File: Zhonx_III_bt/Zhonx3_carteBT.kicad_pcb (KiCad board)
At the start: 2 copper layers, 21.7 x 21.3 mm, 14 parts, among them P1 CONN_01X04, U2 SPBT2632C2A, U3 LP2992

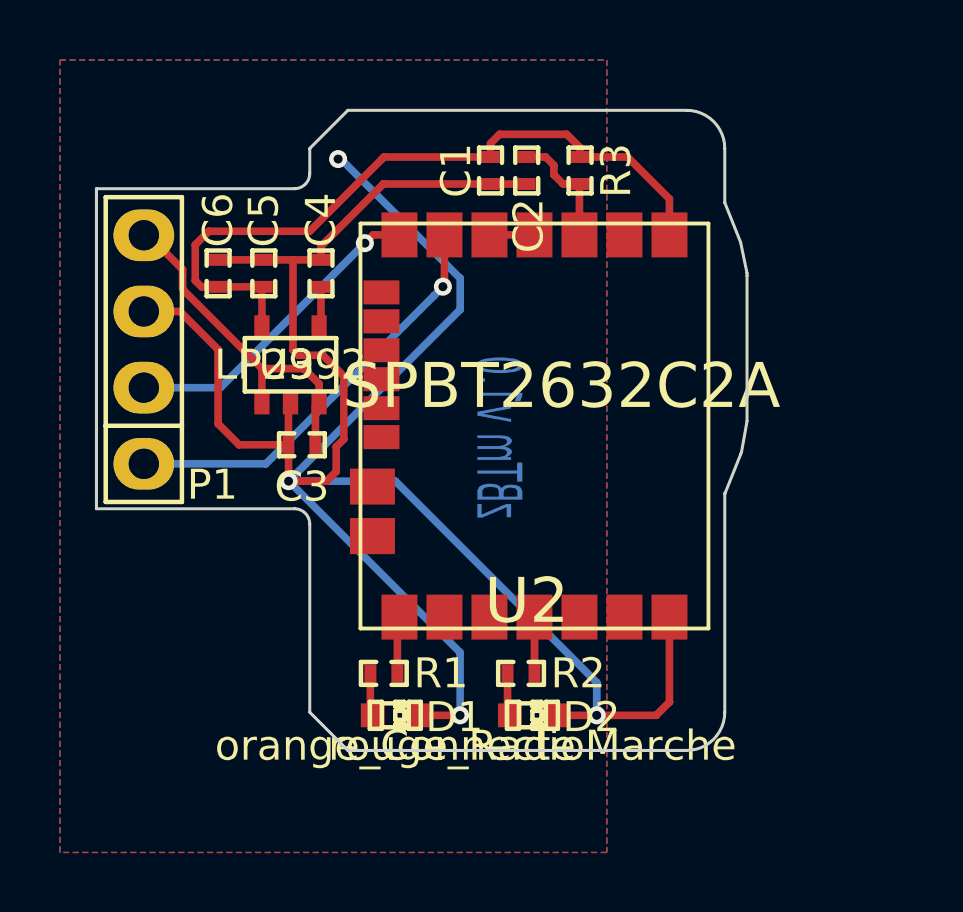
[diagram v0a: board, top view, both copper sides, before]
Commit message: bluetooth passage en 4 couches
Signed-off-by: Jean-Paul <pacabot.jbe@gmail.com>
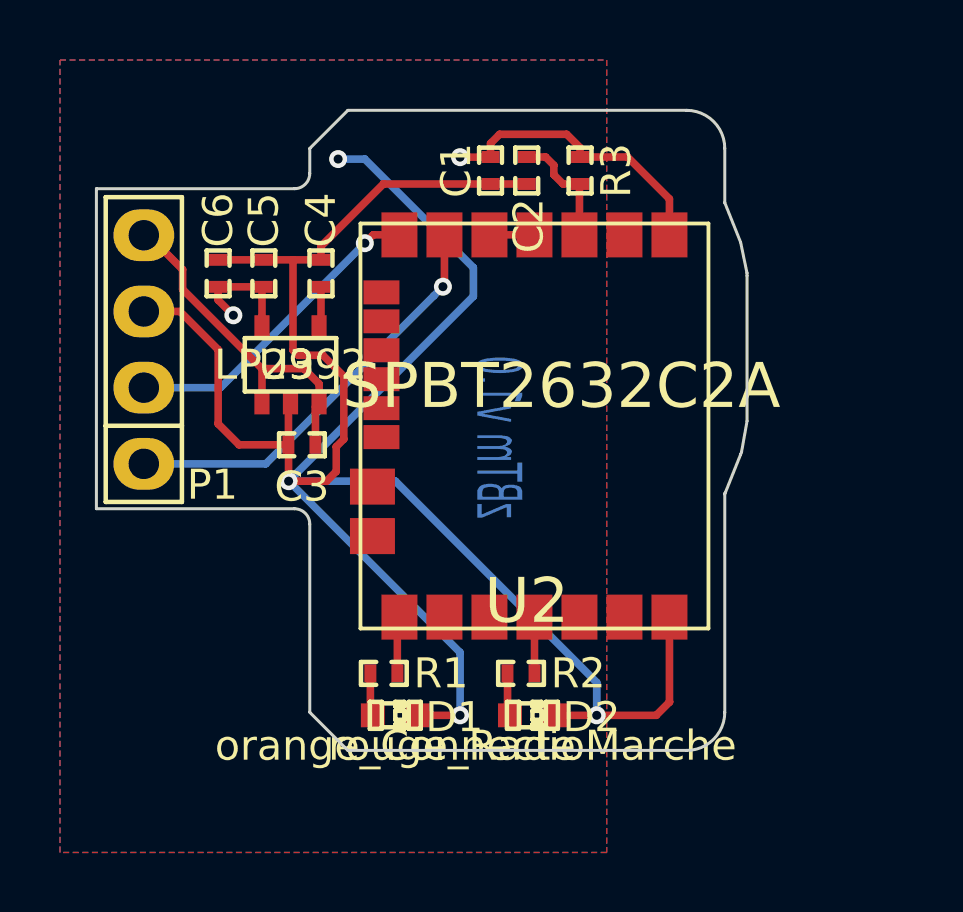
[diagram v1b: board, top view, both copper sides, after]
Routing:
- net +2.5V: track 24.7 -> 23.5 mm, vias 0 -> 2
- net GND: track 79.9 -> 80.7 mm
- added copper zone on VCC.Cu, net +2.5V
- added copper zone on GND.Cu, net GND
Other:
- copper layers 2 -> 4
